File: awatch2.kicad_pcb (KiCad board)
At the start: 4 copper layers, 86 x 46 mm, 165 parts, among them J101 Conn_01x02, J102 Conn_01x02, J103 Conn_01x02, J104 Conn_01x02, J301 Conn_01x02, J801 Molex 1050170001, J802 Conn_01x06, Q701 FDV301N, SW101 B3S-1000, SW102 B3S-1000, SW103 B3S-1000, SW104 B3S-1000, U1 nRF52840, U301 MAX14690, U401 W25Q128JVPIQTR, U501 BMM150, U502 APDS-9306-065, U503 BMI160, U504 BMP388, U601 SPK0641HT4H-1, U701 AYF531035 (LS013B7DH05), U801 AT93C46DN-SH-T, U802 MCP1703A-3302_SOT223, U803 FT2232HL, U901 DRV2604, X1 ABM11W-32.0000MHZ-8-B1U-T3, Y801 FH1200004

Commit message: Route FTDI.
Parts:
- added C818: .1µF, Capacitor_SMD:C_0603_1608Metric, F.Cu at (67.5, 54.4)
- moved C808 1.80 mm to (69.2, 54.4)
- moved J801 0.94 mm to (46.7, 58.6)
- turned R808 to 180 degrees
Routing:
- net GND: track 0.00 -> 69.7 mm, vias 0 -> 30
- net V33_FTDI: track 0.00 -> 61.1 mm, vias 0 -> 4
- net V18_FTDI: track 0.00 -> 38.9 mm
- net /FTDI USB Debug/NRF_SWDIO: track 0.00 -> 34.5 mm, vias 0 -> 2
- net /FTDI USB Debug/NRF_SWDCLK: track 0.00 -> 27.8 mm
- net +2V8: track 0.00 -> 19.4 mm, vias 0 -> 5
- net Net-(C806-Pad1): track 0.00 -> 19.1 mm, vias 0 -> 2
- net Net-(C804-Pad1): track 0.00 -> 16.2 mm, vias 0 -> 2
- net VBUS: track 0.00 -> 15.0 mm
- net /FTDI USB Debug/UARTDBG_TX: track 0.00 -> 12.4 mm
- net /FTDI USB Debug/EECLK: track 0.00 -> 12.3 mm
- net /FTDI USB Debug/EEDATA: track 0.00 -> 11.3 mm
- net /FTDI USB Debug/UARTDBG_RX: track 0.00 -> 11.3 mm
- net /FTDI USB Debug/EECS: track 0.00 -> 11.0 mm
- net /FTDI USB Debug/USB_D-: track 0.00 -> 10.8 mm
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- added copper zone on In2.Cu, net +2V8

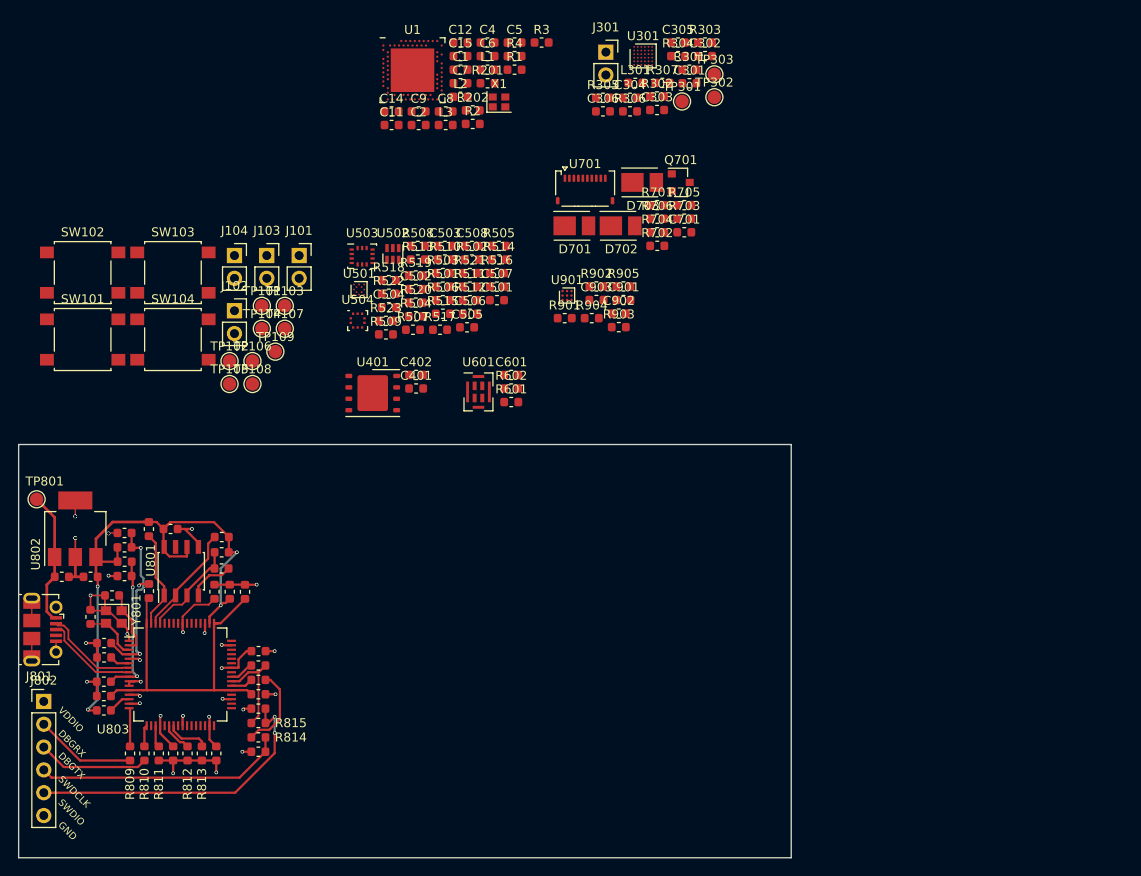
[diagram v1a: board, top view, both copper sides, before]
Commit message: PMIC relative placement and routing
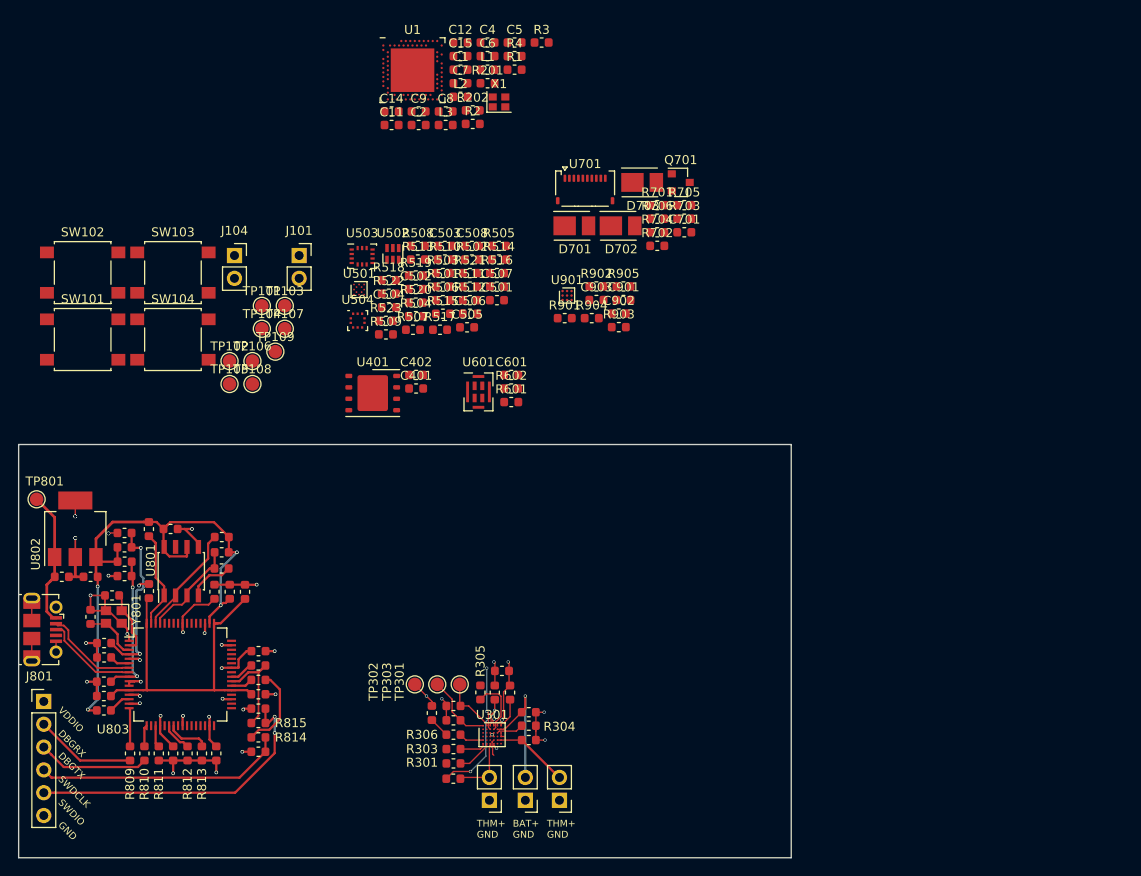
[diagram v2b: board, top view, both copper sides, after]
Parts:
- J102, J103, J301: footprint Connector_PinSocket_2.54mm:PinSocket_1x02_P2.54mm_Vertical -> Connector_PinHeader_2.54mm:PinHeader_1x02_P2.54mm_Vertical
- moved R303 83.5 mm to (92.4, 71.9), turned to 180 degrees
- moved J301 83.4 mm to (104.2, 77.6), turned to 180 degrees
- moved R301 81.6 mm to (92.4, 73.5), turned to 180 degrees
- moved R307 80.9 mm to (92.4, 75.2)
- moved U301 77.4 mm to (96.7, 70.3)
- moved R304 76.4 mm to (100.8, 69.3)
- moved C302 75.6 mm to (100.8, 67.8)
- moved C301 75.3 mm to (100.8, 70.9)
- moved TP303 74.6 mm to (90.6, 64.7)
- moved TP302 73.4 mm to (88.1, 64.7)
- moved R302 73.1 mm to (90.0, 67.9), turned to 90 degrees
- moved C305 72.6 mm to (97.8, 63.2), turned to 180 degrees
- moved R306 72.1 mm to (92.4, 70.3), turned to 180 degrees
- moved C304 70.5 mm to (92.4, 67.1), turned to 180 degrees
- moved C306 69.8 mm to (92.4, 68.7), turned to 180 degrees
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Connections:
- net Net-(C301-Pad1) renamed /PMIC/MAX_CHGIN
- net Net-(C303-Pad2) renamed /PMIC/MAX_CAP
- net Net-(L301-Pad1) renamed /PMIC/MAX_B2LX
- net Net-(R301-Pad1) renamed /PMIC/MAX_SCL
- net Net-(R303-Pad1) renamed /PMIC/MAX_SDA
- net Net-(R304-Pad1) renamed /PMIC/MAX_SET
- net Net-(R305-Pad1) renamed /PMIC/MAX_MON
- net Net-(R306-Pad1) renamed /PMIC/MAX_RSTN
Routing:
- net /PMIC/BAT+: track 0.00 -> 14.5 mm, vias 0 -> 1
- net /PMIC/MAX_CAP: track 0.00 -> 14.1 mm, vias 0 -> 2
- net GND: track 69.7 -> 82.6 mm, vias 30 -> 37
- net +2V8: track 19.4 -> 30.4 mm, vias 5 -> 8
- net /PMIC/MAX_CHGIN: track 0.00 -> 8.62 mm
- net +3.3V: track 0.00 -> 7.83 mm
- net +3V8: track 0.00 -> 7.18 mm
- net /PMIC/BAT_THM: track 0.00 -> 7.08 mm
- net /PMIC/PMIC_INTn: track 0.00 -> 6.97 mm, vias 0 -> 2
- net /PMIC/MAX_MON: track 0.00 -> 6.67 mm
- net /PMIC/MAX_SCL: track 0.00 -> 4.00 mm
- net /PMIC/MAX_B2LX: track 0.00 -> 3.43 mm
- net /PMIC/MAX_SET: track 0.00 -> 3.03 mm
- net /PMIC/MAX_SDA: track 0.00 -> 2.94 mm
- net /PMIC/MAX_RSTN: track 0.00 -> 2.76 mm
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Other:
- net class MAX14690 added: clearance 0.127, trace_width 0.06985, via_dia 0.3556, via_drill 0.254
- board text added: "BAT+ GND"
- board text added: "THM+ GND"

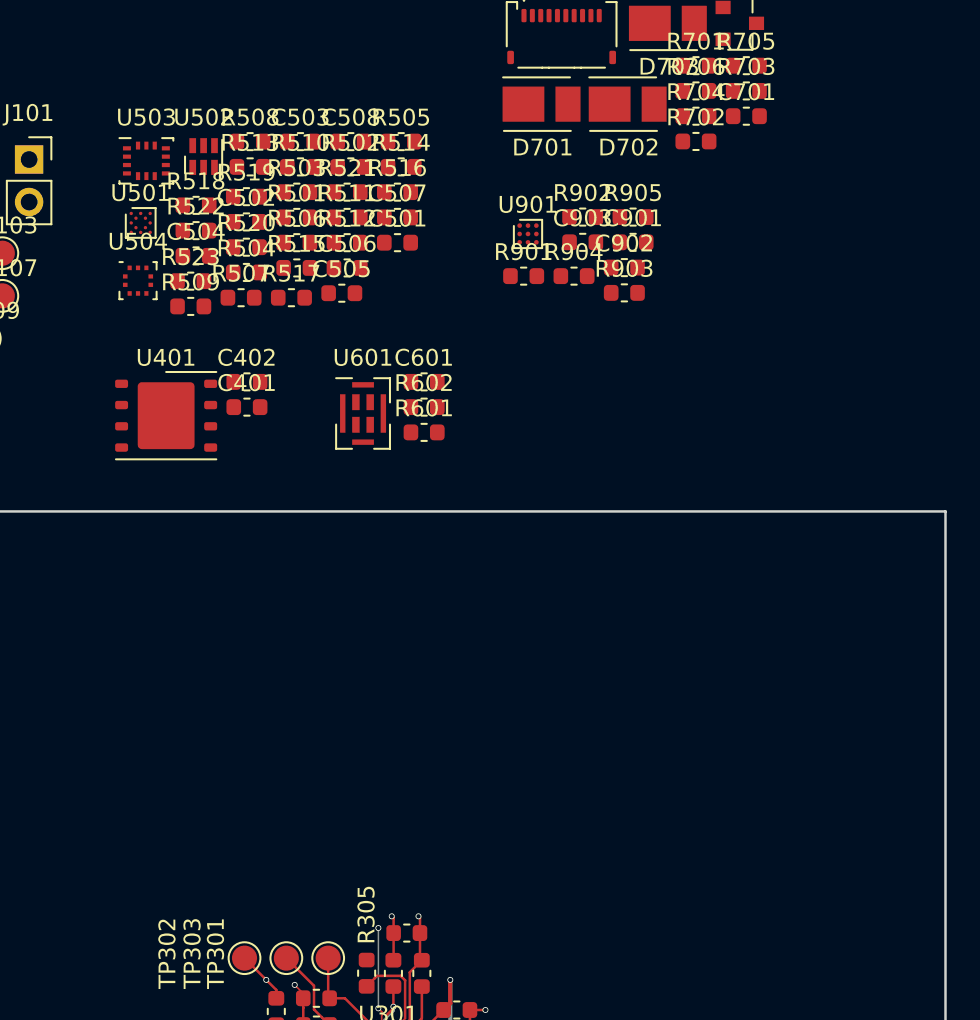
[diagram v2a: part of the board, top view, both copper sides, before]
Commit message: place and route ambient light sensor
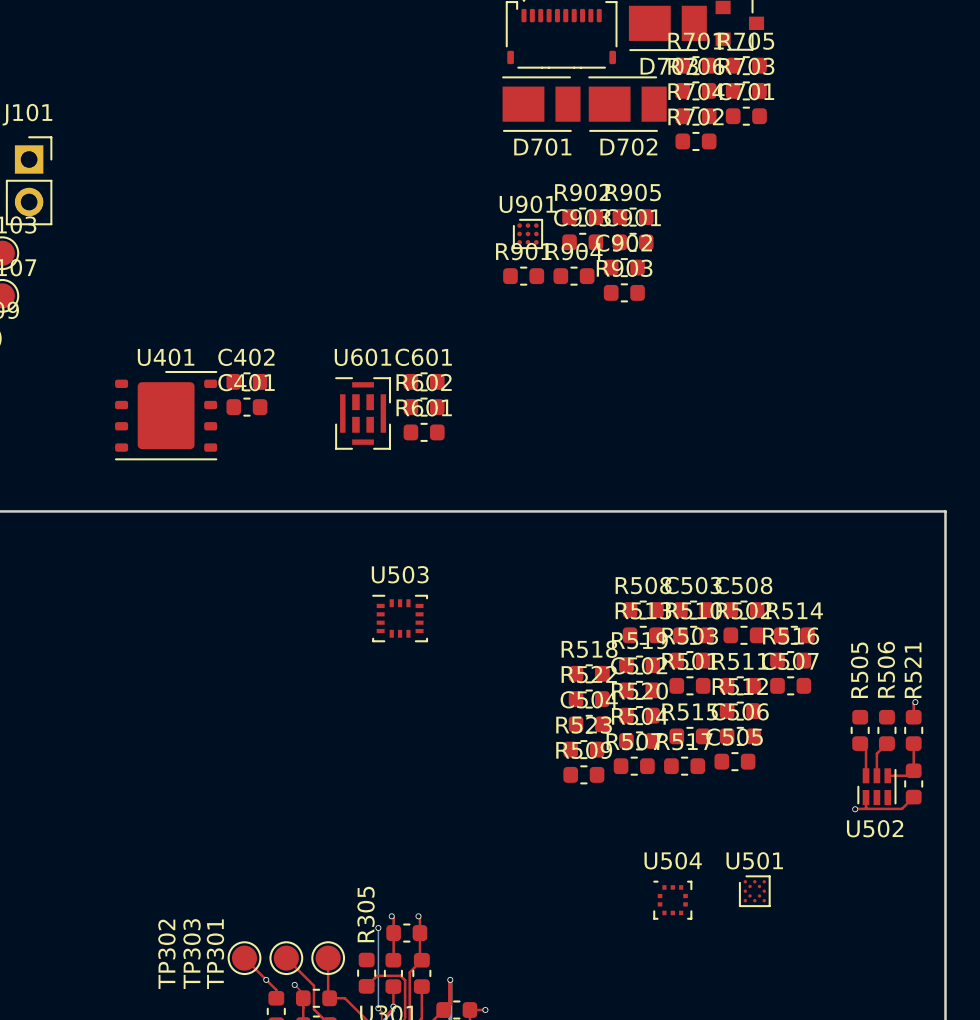
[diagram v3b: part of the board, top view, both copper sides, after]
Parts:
- moved U502 55.1 mm to (125.9, 54.5)
- moved U501 54.2 mm to (118.6, 60.7)
- moved U504 48.9 mm to (113.7, 61.2)
- moved R521 46.7 mm to (128.1, 51.1), turned to 90 degrees
- moved R506 45.8 mm to (126.5, 51.1), turned to 90 degrees
- moved C501 44.7 mm to (128.1, 54.3), turned to 270 degrees
- moved R505 44.6 mm to (124.9, 51.1), turned to 90 degrees
- moved C503 36.6 mm to (114.9, 43.9)
- moved C504 36.6 mm to (108.7, 50.7)
- moved C505 36.6 mm to (117.4, 53.0)
- moved C507 36.6 mm to (120.7, 48.4)
- moved C508 36.6 mm to (118.0, 43.9)
- moved R501 36.6 mm to (114.7, 48.4)
- moved R502 36.6 mm to (118.0, 45.4)
- moved R504 36.6 mm to (111.7, 51.7)
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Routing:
- net GND: track 82.6 -> 87.1 mm, vias 37 -> 38
- net Net-(C501-Pad1): track 0.00 -> 3.30 mm
- net Net-(R506-Pad1): track 0.00 -> 2.17 mm
- net Net-(R505-Pad1): track 0.00 -> 2.07 mm
- net +2V8: track 30.4 -> 31.3 mm, vias 8 -> 9

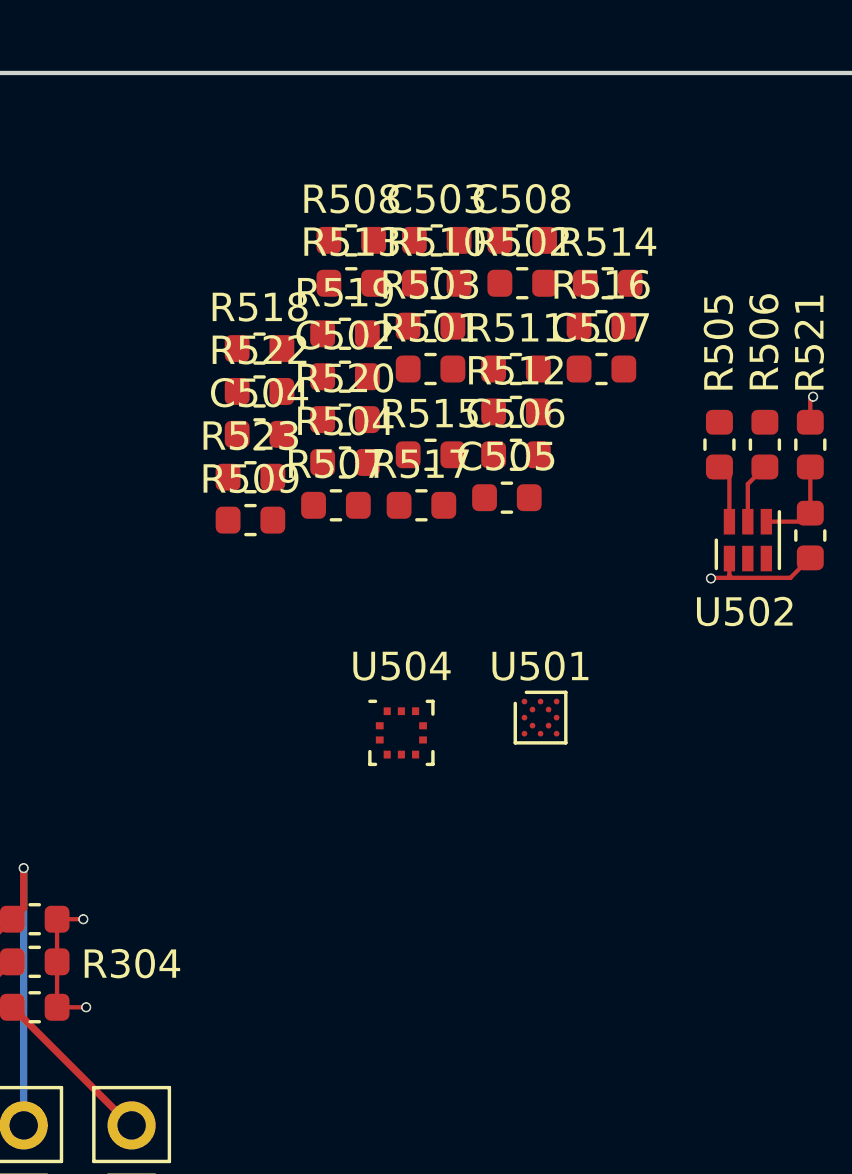
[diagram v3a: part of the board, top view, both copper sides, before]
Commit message: Place and route pressure sensor.
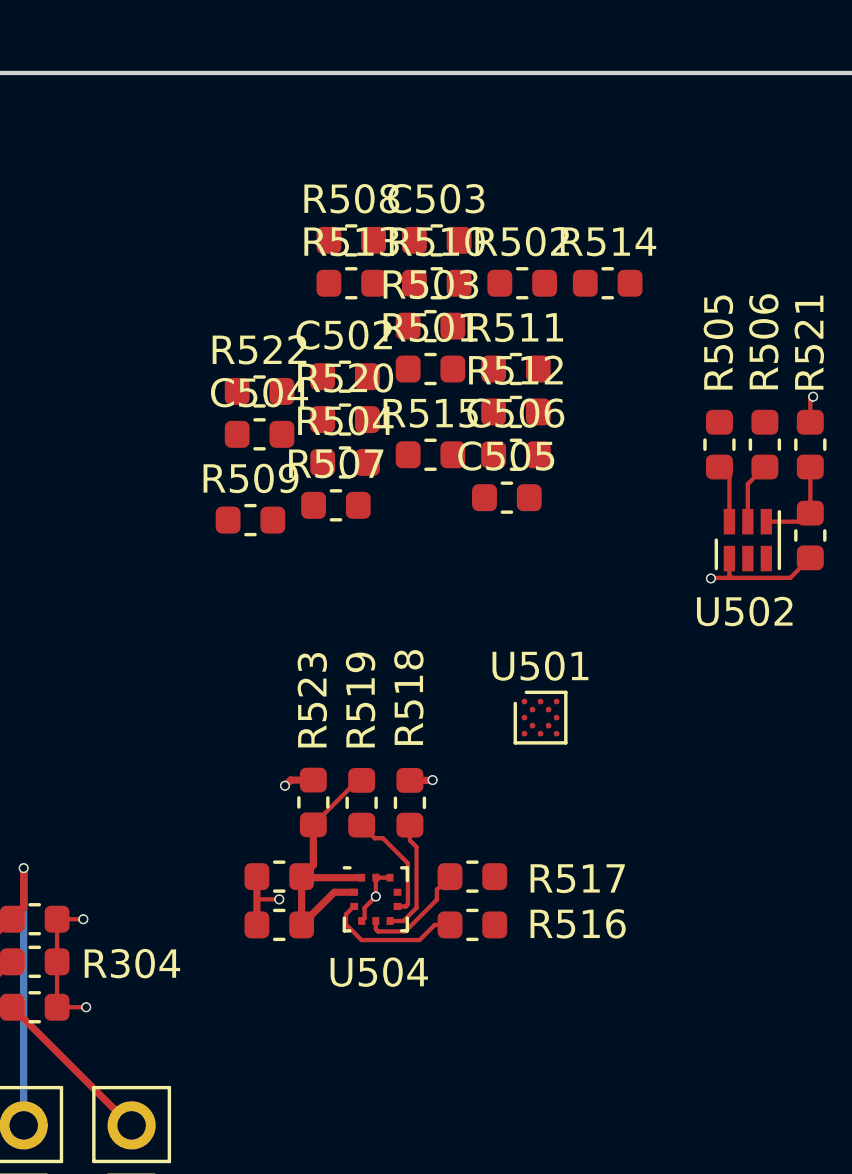
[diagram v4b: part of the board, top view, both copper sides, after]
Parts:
- moved C508 25.6 mm to (109.4, 68.0), turned to 180 degrees
- moved R516 21.6 mm to (116.2, 68.0)
- moved C507 21.2 mm to (109.4, 66.3), turned to 180 degrees
- moved R518 16.8 mm to (114.0, 63.7), turned to 270 degrees
- moved R519 16.5 mm to (112.3, 63.7), turned to 90 degrees
- moved R517 13.2 mm to (116.2, 66.3)
- moved R523 11.7 mm to (110.6, 63.7), turned to 90 degrees
- moved U504 5.93 mm to (112.8, 67.1)
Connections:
- U504 pad 3: (no net) -> GND
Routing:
- net Net-(C507-Pad1): track 0.00 -> 10.5 mm
- net GND: track 87.1 -> 94.3 mm, vias 38 -> 41
- net Net-(R516-Pad1): track 0.00 -> 4.87 mm
- net Net-(R518-Pad2): track 0.00 -> 4.13 mm
- net Net-(R519-Pad1): track 0.00 -> 4.03 mm
- net Net-(R517-Pad1): track 0.00 -> 3.94 mm
- net +2V8: track 31.3 -> 32.4 mm, vias 9 -> 10
